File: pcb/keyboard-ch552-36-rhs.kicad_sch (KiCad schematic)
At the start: 55 parts, among them J1 PJ-320A, J1 USB Type-C Receptacle 12-pin, SW1 SW_SPST, SW2 SW_SPST, U1 CH552T

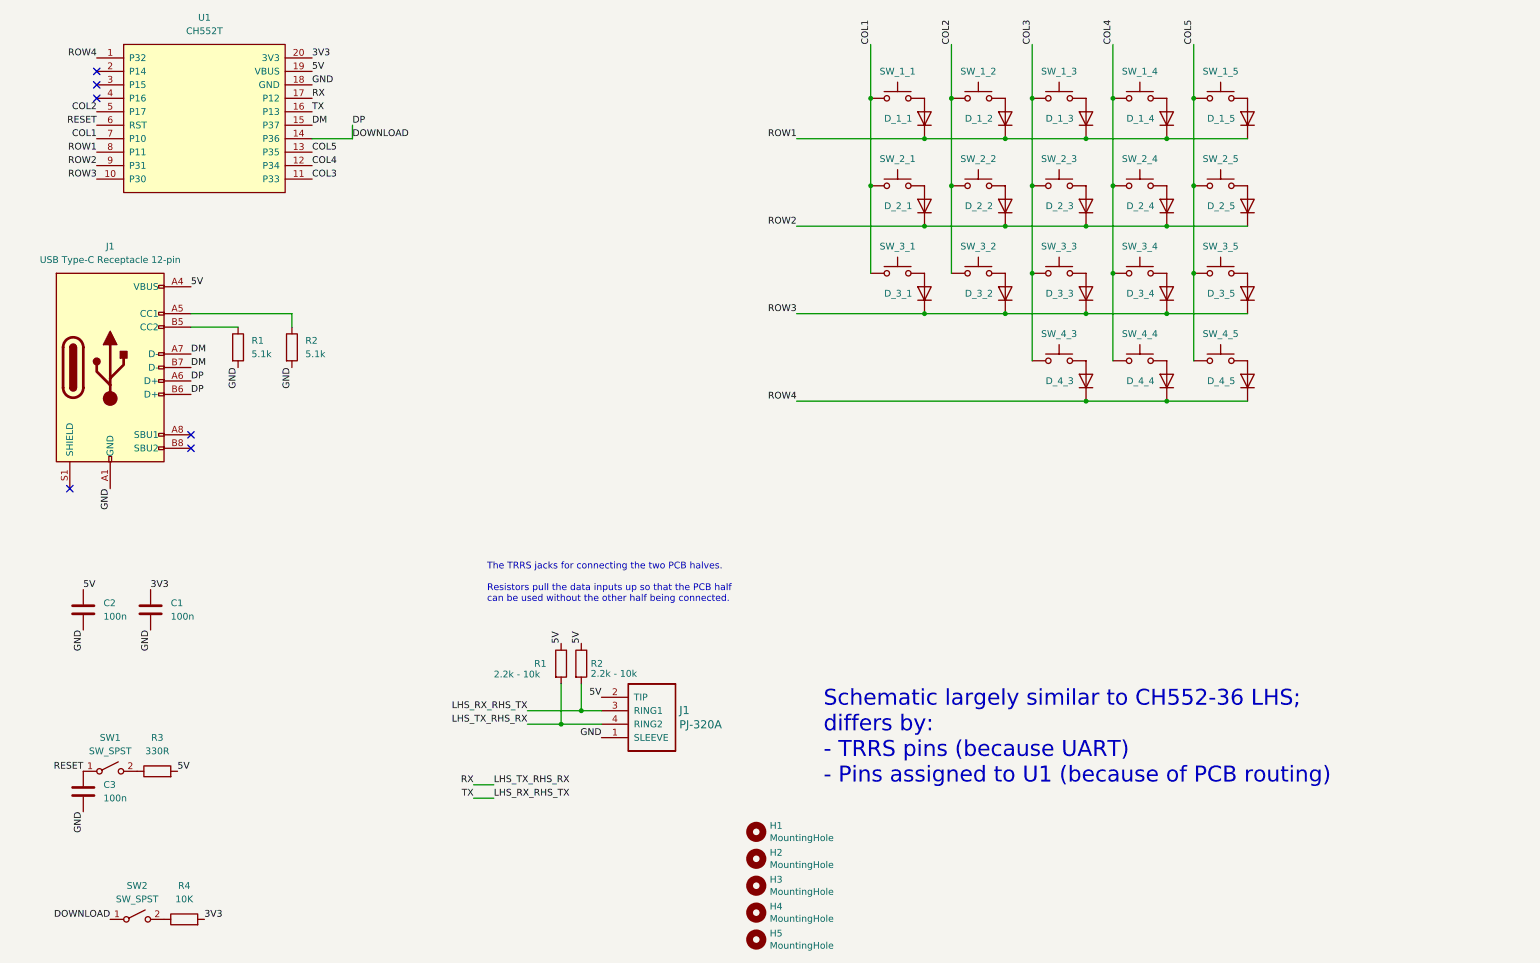
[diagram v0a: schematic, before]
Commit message: pcb: break out SPI pins for ISP flash on CH552-36 RHS
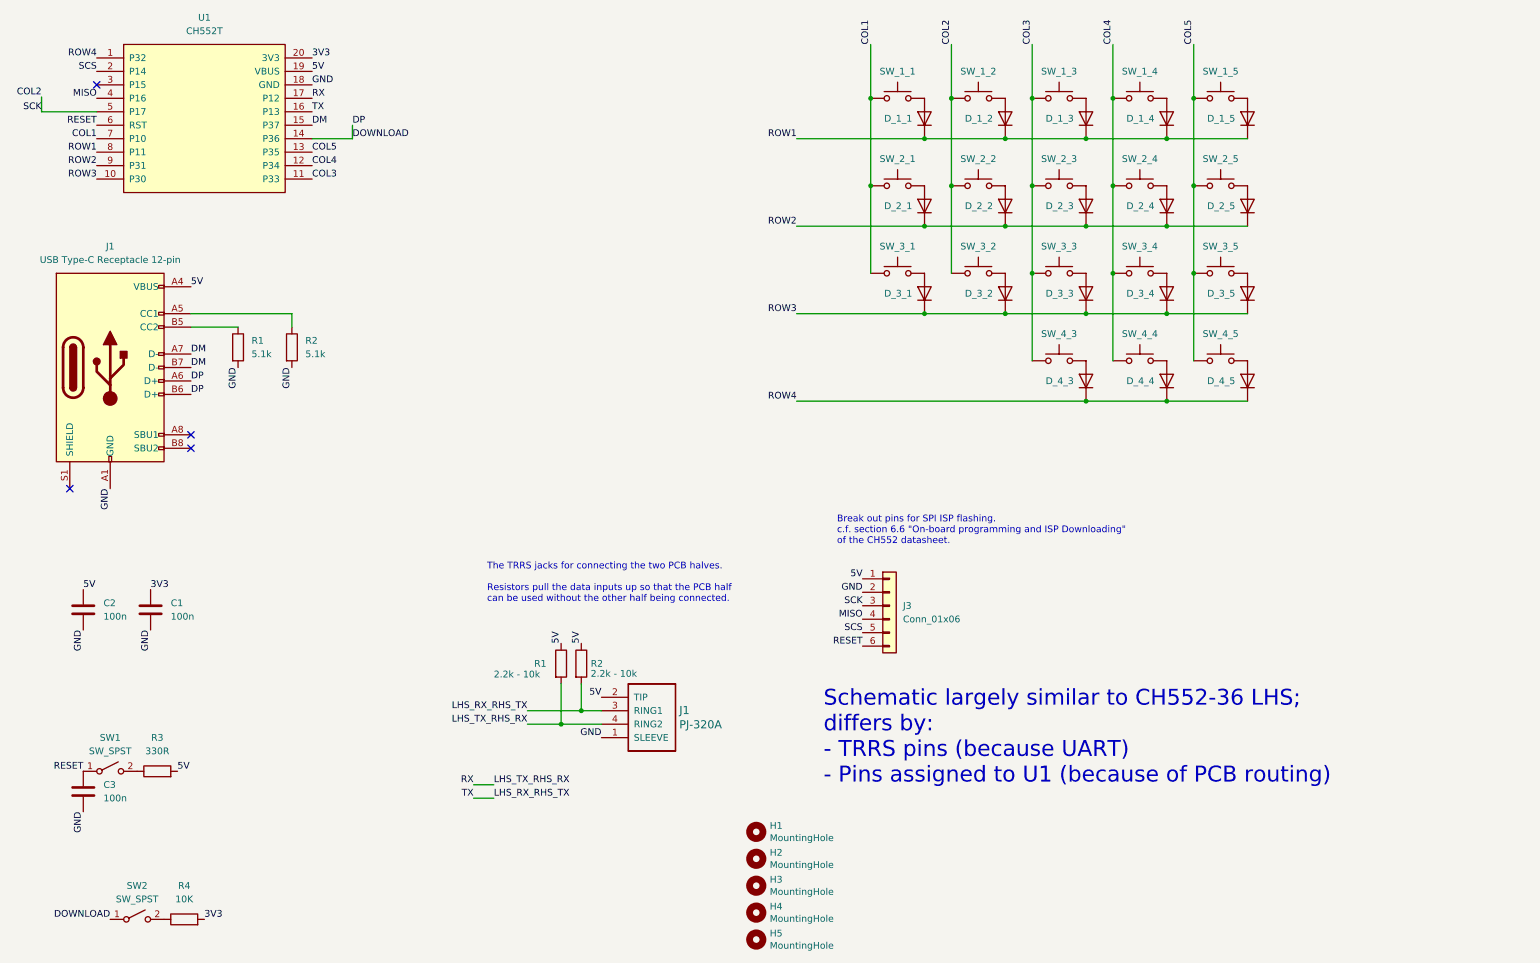
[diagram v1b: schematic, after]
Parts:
- added J3: Conn_01x06, symbol Connector_Generic:Conn_01x06
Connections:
- net 5V: now also J3.1 (Pin_1)
- net COL2: now also J3.3 (Pin_3)
- net GND: now also J3.2 (Pin_2)
- net RESET: now also J3.6 (Pin_6)
- net SCS: now reaches U1.2 (P14)
- net SCS: now also J3.5 (Pin_5)
- net MISO: now reaches U1.4 (P16)
- net MISO: now also J3.4 (Pin_4)
- no-connect marks 6 -> 4
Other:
- note added: "Break out pins for SPI ISP flashing. c.f. section 6.6 "On-board programming and ISP Downloading" of the CH552 datasheet."
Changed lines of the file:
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@@
   (title_block
     (title "CH552-36 (RHS)")
-    (date "2023-12-16")
-    (rev "rev2023.1")
+    (date "2024-01-03")
+    (rev "rev2024.1-pre")
     (company "Richard Goulter (rgoulter)")
     (comment 1 "Using CH552T MCU.")
@@
   )
   (no_connect (at 31.75 29.21))
-  (no_connect (at 31.75 26.67))
   (no_connect (at 26.67 105.41))
   (no_connect (at 49.53 95.25))
-  (no_connect (at 31.75 31.75))
   (no_connect (at 49.53 97.79))
   (wire (pts (xy 223.52 21.59) (xy 223.52 31.75))
@@
     (stroke (width 0) (type default))
   )
+  (wire (pts (xy 21.336 34.29) (xy 31.75 34.29))
+    (stroke (width 0) (type default))
+  )
   (wire (pts (xy 218.44 55.88) (xy 233.68 55.88))
     (stroke (width 0) (type default))
@@
   )
   (wire (pts (xy 163.83 88.9) (xy 218.44 88.9))
+    (stroke (width 0) (type default))
+  )
+  (wire (pts (xy 21.336 31.496) (xy 21.336 34.29))
     (stroke (width 0) (type default))
   )
@@
     (effects (font (size 1.27 1.27)) (justify left bottom))
   )
+  (text "Break out pins for SPI ISP flashing.\nc.f. section 6.6 \"On-board programming and ISP Downloading\"\nof the CH552 datasheet."
+    (at 171.45 116.078 0)
+    (effects (font (size 1.27 1.27)) (justify left bottom))
+  )
+  (label "SCS" (at 31.75 26.67 180) (fields_autoplaced)
+    (effects (font (size 1.27 1.27)) (justify right bottom))
+  )
   (label "3V3" (at 72.39 24.13 0) (fields_autoplaced)
     (effects (font (size 1.27 1.27)) (justify left bottom))
   )
+  (label "SCK" (at 21.336 34.29 180) (fields_autoplaced)
+    (effects (font (size 1.27 1.27)) (justify right bottom))
+  )
   (label "COL4" (at 223.52 21.59 90) (fields_autoplaced)
     (effects (font (size 1.27 1.27)) (justify left bottom))
@@
     (effects (font (size 1.27 1.27)) (justify right bottom))
   )
+  (label "SCS" (at 176.276 132.588 180) (fields_autoplaced)
+    (effects (font (size 1.27 1.27)) (justify right bottom))
+  )
   (label "RESET" (at 29.21 158.75 180) (fields_autoplaced)
     (effects (font (size 1.27 1.27)) (justify right bottom))
@@
     (effects (font (size 1.27 1.27)) (justify left bottom))
   )
+  (label "MISO" (at 31.75 31.75 180) (fields_autoplaced)
+    (effects (font (size 1.27 1.27)) (justify right bottom))
+  )
   (label "TX" (at 102.87 163.83 180) (fields_autoplaced)
     (effects (font (size 1.27 1.27)) (justify right bottom))
@@
     (effects (font (size 1.27 1.27)) (justify left bottom))
   )
+  (label "GND" (at 176.276 124.968 180) (fields_autoplaced)
+    (effects (font (size 1.27 1.27)) (justify right bottom))
+  )
   (label "COL3" (at 208.28 21.59 90) (fields_autoplaced)
     (effects (font (size 1.27 1.27)) (justify left bottom))
@@
     (effects (font (size 1.27 1.27)) (justify right bottom))
   )
-  (label "COL2" (at 31.75 34.29 180) (fields_autoplaced)
+  (label "COL2" (at 21.336 31.496 180) (fields_autoplaced)
     (effects (font (size 1.27 1.27)) (justify right bottom))
   )
@@
     (effects (font (size 1.27 1.27)) (justify right bottom))
   )
+  (label "MISO" (at 176.276 130.048 180) (fields_autoplaced)
+    (effects (font (size 1.27 1.27)) (justify right bottom))
+  )
   (label "GND" (at 34.29 105.41 270) (fields_autoplaced)
     (effects (font (size 1.27 1.27)) (justify right bottom))
@@
     (effects (font (size 1.27 1.27)) (justify left bottom))
   )
+  (label "RESET" (at 176.276 135.128 180) (fields_autoplaced)
+    (effects (font (size 1.27 1.27)) (justify right bottom))
+  )
   (label "TX" (at 72.39 34.29 0) (fields_autoplaced)
     (effects (font (size 1.27 1.27)) (justify left bottom))
@@
   (label "DM" (at 49.53 80.01 0) (fields_autoplaced)
     (effects (font (size 1.27 1.27)) (justify left bottom))
+  )
+  (label "5V" (at 176.276 122.428 180) (fields_autoplaced)
+    (effects (font (size 1.27 1.27)) (justify right bottom))
+  )
+  (label "SCK" (at 176.276 127.508 180) (fields_autoplaced)
+    (effects (font (size 1.27 1.27)) (justify right bottom))
   )
   (label "5V" (at 72.39 26.67 0) (fields_autoplaced)
@@
         )
       )
+    )
+  )
+  (symbol (lib_id "Connector_Generic:Conn_01x06") (at 181.356 127.508 0) (unit 1)
+    (in_bom yes) (on_board yes) (dnp no) (fields_autoplaced)
+    (property "Reference" "J3" (at 183.896 127.508 0)
+      (effects (font (size 1.27 1.27)) (justify left))
+    )
+    (property "Value" "Conn_01x06" (at 183.896 130.048 0)
+      (effects (font (size 1.27 1.27)) (justify left))
+    )
+    (property "Footprint" "" (at 181.356 127.508 0)
+      (effects (font (size 1.27 1.27)) hide)
+    )
+    (property "Datasheet" "~" (at 181.356 127.508 0)
+      (effects (font (size 1.27 1.27)) hide)
+    )
+    (pin "1")
+    (pin "2")
+    (pin "3")
+    (pin "4")
+    (pin "5")
+    (pin "6")
+    (instances
+      (project "keyboard-ch552-36-rhs"
+        (path "/491af640-c615-48ab-84d8-9b166bc1ab37"
+          (reference "J3") (unit 1)
+        )
+      )
